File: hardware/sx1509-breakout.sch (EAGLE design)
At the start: 23 parts, among them U1 SX1509

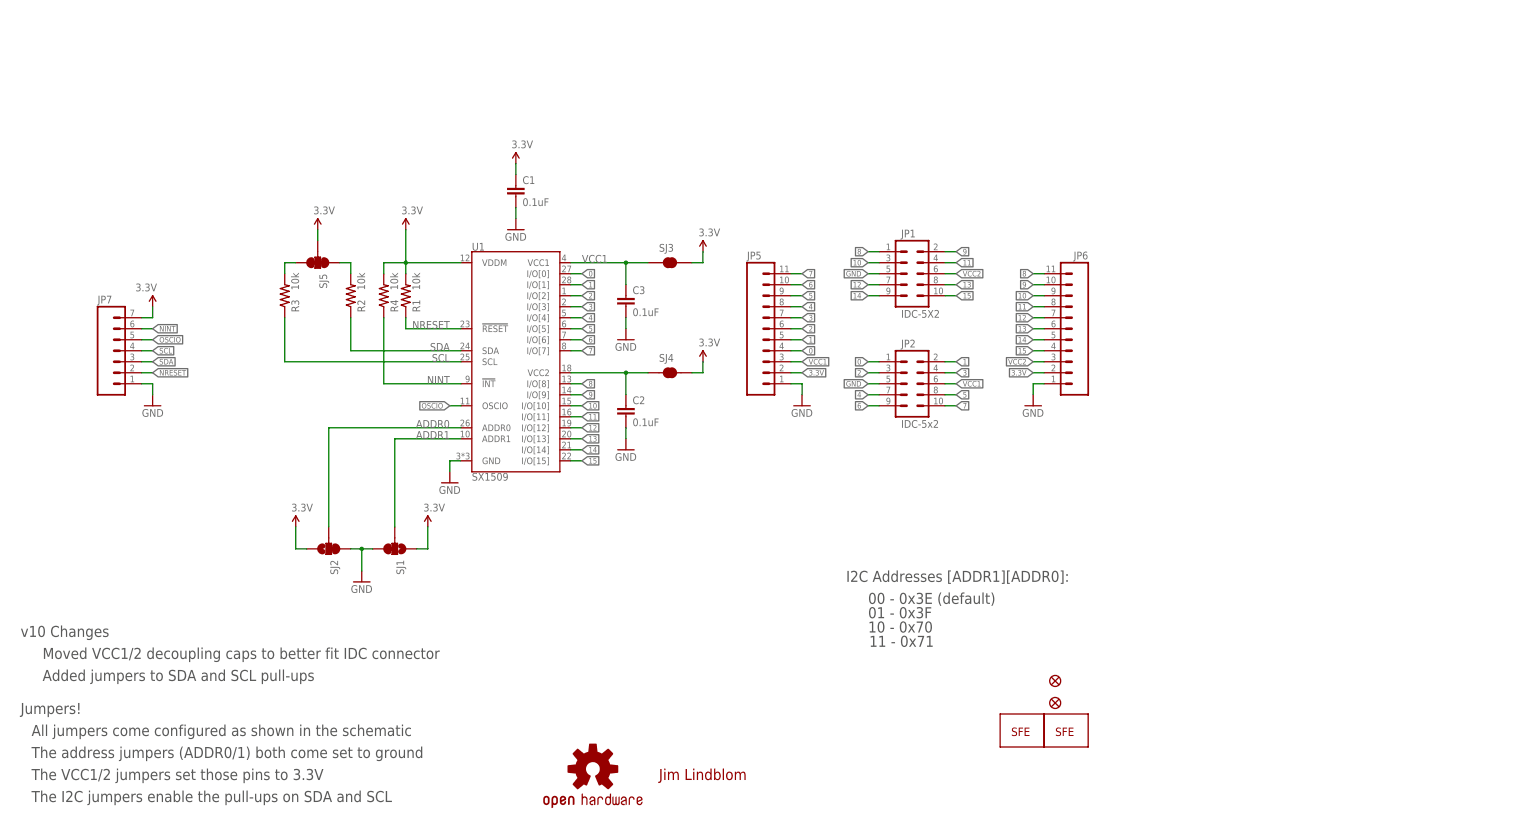
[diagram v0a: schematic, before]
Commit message: Initial commit of v1.1
- Added standoff holes
- Changed I2C headers to match SparkFun standard
- Added I2C pins to both sides to allow cascading boards.
- Updated Eagle libraries
- Updated 0402 packages to 0603.
- Increase fiducial size
- Updated logos
- Added 10k resistors to SJ2 and SJ3.
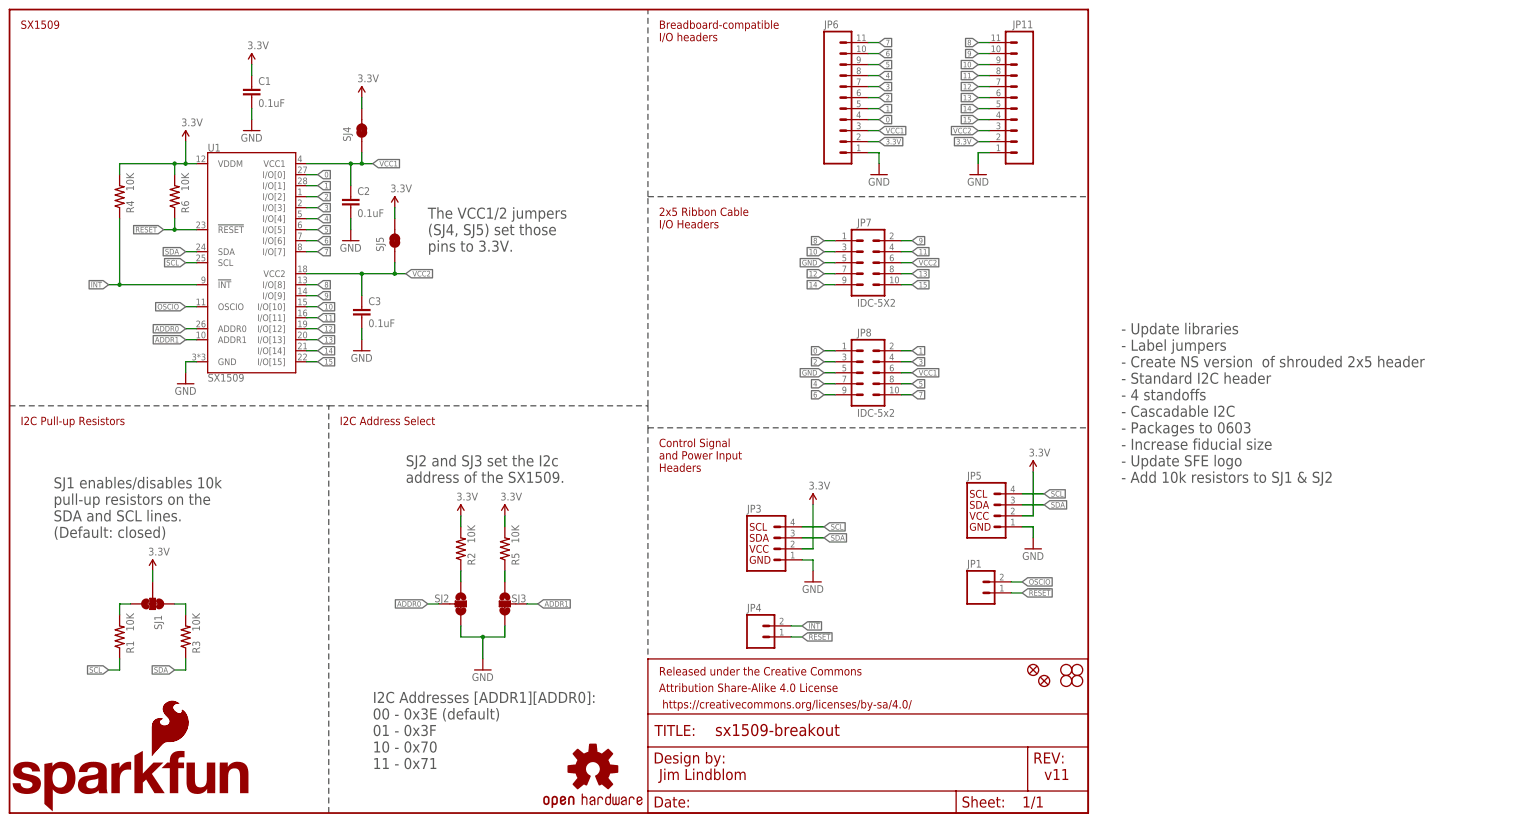
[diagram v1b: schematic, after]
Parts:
- removed JP2: IDC-5x2, SparkFun-Connectors:M05X2SHD_NS
- added FRAME1: (no value), SparkFun-Aesthetics:FRAME-LETTER
- added JP10: FIDUCIAL1X2, SparkFun:FIDUCIAL1X2
- added JP11: (no value), SparkFun-Connectors:M111X11_NO_SILK
- added LOGO1: SFE_LOGO_NAME_FLAME.1_INCH, SparkFun-Aesthetics:SFE_LOGO_NAME_FLAME.1_INCH
- added LOGO2: SFE_LOGO_FLAME.1_INCH, SparkFun-Aesthetics:SFE_LOGO_FLAME.1_INCH
- added R5, R6: 10K, SparkFun-Resistors:10KOHM-1/10W-1%(0603)0603
- added STANDOFF1, STANDOFF2, STANDOFF3, STANDOFF4: STAND-OFF, SparkFun-Electromechanical:STAND-OFF
- C1, C2, C3: device SparkFun-Passives:CAP0402-CAP -> SparkFun-Capacitors:0.1UF-25V(+80/-20%)(0603)
- JP1: value IDC-5X2 -> (none); device SparkFun-Connectors:M05X2SHD_NS -> SparkFun-Connectors:M021X02_NO_SILK
- JP3: value LOGO-SFENEW -> (none); device SparkFun-Aesthetics:LOGO-SFENEW -> SparkFun-Connectors:I2C_STANDARD_NO_SILK
- JP4: value LOGO-SFESK -> (none); device SparkFun-Aesthetics:LOGO-SFESK -> SparkFun-Connectors:M021X02_NO_SILK
- JP5: value M111X11_NO_SILK -> (none); device SparkFun-Connectors:M111X11_NO_SILK -> SparkFun-Connectors:I2C_STANDARD_NO_SILK
- JP6: value M111X11_NO_SILK -> (none)
- JP7: value (none) -> IDC-5X2; device SparkFun-Connectors:M07 -> SparkFun-Connectors:M05X2SHD-NS
- JP8: value FIDUCIALUFIDUCIAL -> IDC-5x2; device SparkFun:FIDUCIALUFIDUCIAL -> SparkFun-Connectors:M05X2SHD-NS
- JP9: value FIDUCIALUFIDUCIAL -> FIDUCIAL1X2; device SparkFun:FIDUCIALUFIDUCIAL -> SparkFun:FIDUCIAL1X2
- R1, R2, R3, R4: value 10k -> 10K; device SparkFun-Passives:RESISTOR0402-RES -> SparkFun-Resistors:10KOHM-1/10W-1%(0603)0603
- SJ1: device SparkFun-Passives:SOLDERJUMPER_2WAYS -> SparkFun-Passives:JUMPER-PAD-3-NC_BY_TRACE
- SJ2: value (none) -> JUMPER-PAD-3-2OF3_NC_BY_TRACE_SMALL; device SparkFun-Passives:SOLDERJUMPER_2WAYS -> SparkFun-Passives:JUMPER-PAD-3-2OF3_NC_BY_TRACE_SMALL
- SJ3: value SOLDERJUMPERNO -> JUMPER-PAD-3-2OF3_NC_BY_TRACE_SMALL; device SparkFun-Passives:SOLDERJUMPERNO -> SparkFun-Passives:JUMPER-PAD-3-2OF3_NC_BY_TRACE_SMALL
- SJ4: value SOLDERJUMPERNO -> JUMPER-PAD-2-NC_BY_TRACE; device SparkFun-Passives:SOLDERJUMPERNO -> SparkFun-Passives:JUMPER-PAD-2-NC_BY_TRACE
- SJ5: value (none) -> JUMPER-PAD-2-NC_BY_TRACE; device SparkFun-Passives:SOLDERJUMPER_2WAYS -> SparkFun-Passives:JUMPER-PAD-2-NC_BY_TRACE
- renumbered U$1 to LOGO3
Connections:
- removed net NINT: JP7.6, R4.1, U1.!INT
- removed net NRESET: JP7.2, R1.1, U1.!RESET
- new net !INT: JP4.2, R4.1, U1.!INT
- new net !RESET: JP1.1, JP4.1, R6.1, U1.!RESET
- new net N$8: R2.1, SJ2.1
- new net N$9: R5.1, SJ3.1
- net 0: now also JP6.4, JP8.1; no longer JP2.1, JP5.4
- net 1: now also JP6.5, JP8.2; no longer JP2.2, JP5.5
- net 10: now also JP11.9, JP7.3; no longer JP1.3, JP6.9
- net 11: now also JP11.8, JP7.4; no longer JP1.4, JP6.8
- net 12: now also JP11.7, JP7.7; no longer JP1.7, JP6.7
- net 13: now also JP11.6, JP7.8; no longer JP1.8, JP6.6
- net 14: now also JP11.5, JP7.9; no longer JP1.9, JP6.5
- net 15: now also JP11.4, JP7.10; no longer JP1.10, JP6.4
- net 2: now also JP6.6, JP8.3; no longer JP2.3, JP5.6
- net 3: now also JP6.7, JP8.4; no longer JP2.4, JP5.7
- net 3.3V: now also JP11.2, JP3.2, R2.2, R5.2, R6.2, SJ1.2; no longer JP7.7, R1.2, SJ1.1, SJ2.3, SJ3.2
- net 4: now also JP6.8, JP8.7; no longer JP2.7, JP5.8
- net 5: now also JP6.9, JP8.8; no longer JP2.8, JP5.9
- net 6: now also JP6.10, JP8.9; no longer JP2.9, JP5.10
- net 7: now also JP6.11, JP8.10; no longer JP2.10, JP5.11
- net 8: now also JP11.11, JP7.1; no longer JP1.1, JP6.11
- net 9: now also JP11.10, JP7.2; no longer JP1.2, JP6.10
- net ADDR1: now also SJ3.2; no longer SJ1.2
- net GND: now also JP11.1, JP3.1, JP7.5, JP8.5, SJ2.3, SJ3.3; no longer JP1.5, JP2.5, JP7.1, SJ1.3, SJ2.1
- net N$1: now also R1.2, SJ1.3; no longer R3.2, SJ5.3
- net N$2: now also R3.2, SJ1.1; no longer R2.2, SJ5.1
- net OSCIO: now also JP1.2; no longer JP7.5
- net SCL: now also JP3.4, JP5.4, R1.1; no longer JP7.4, R3.1
- net SDA: now also JP3.3, JP5.3, R3.1; no longer JP7.3, R2.1
- net VCC1: now also C2.1, JP6.3, JP8.6, SJ4.1; no longer C3.1, JP2.6, JP5.3, SJ3.1
- net VCC2: now also C3.1, JP11.3, JP7.6, SJ5.1; no longer C2.1, JP1.6, JP6.3, SJ4.1
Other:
- note added: "- Update libraries - Label jumpers - Create NS version of shrouded 2x5 header - Standard I2C header - 4 standoffs - Cascadable I2C - Packages to 0603 - Increase fiducial size - Update SFE logo - Add 10k resistors to SJ1 & SJ2"
- note added: "2x5 Ribbon Cable I/O Headers"
- note added: "Breadboard-compatible I/O headers"
- note added: "Control Signal and Power Input Headers"
- note added: "I2C Address Select"
- note added: "I2C Addresses [ADDR1][ADDR0]: 00 - 0x3E (default) 01 - 0x3F 10 - 0x70 11 - 0x71"
- note added: "I2C Pull-up Resistors"
- note added: "SJ1 enables/disables 10k pull-up resistors on the SDA and SCL lines. (Default: closed)"
- note added: "SJ2 and SJ3 set the I2c address of the SX1509."
- note added: "SX1509"
- note added: "The VCC1/2 jumpers (SJ4, SJ5) set those pins to 3.3V."
- note added: "v11"
- note removed: "00 - 0x3E (default)"
- note removed: "01 - 0x3F"
- note removed: "10 - 0x70"
- note removed: "11 - 0x71"
- note removed: "Added jumpers to SDA and SCL pull-ups"
- note removed: "All jumpers come configured as shown in the schematic"
- note removed: "I2C Addresses [ADDR1][ADDR0]:"
- note removed: "Jumpers!"
- note removed: "Moved VCC1/2 decoupling caps to better fit IDC connector"
- note removed: "The I2C jumpers enable the pull-ups on SDA and SCL"
- note removed: "The VCC1/2 jumpers set those pins to 3.3V"
- note removed: "The address jumpers (ADDR0/1) both come set to ground"
- note removed: "v10 Changes"
- moved on the sheet: C1, C2, C3, JP6, R1, R2, R3, R4, U1

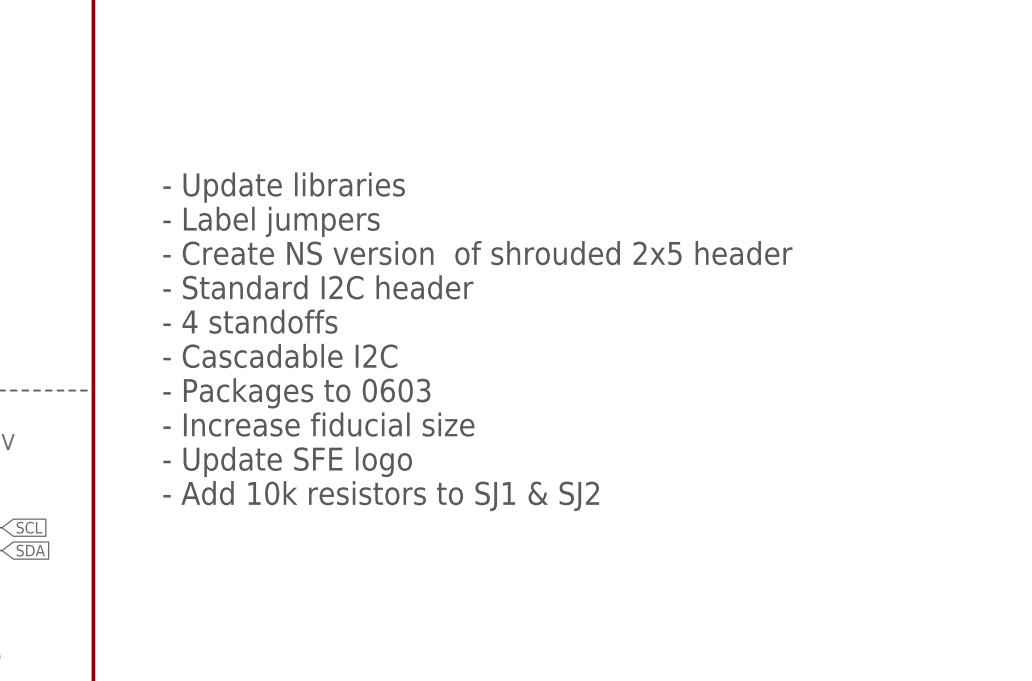
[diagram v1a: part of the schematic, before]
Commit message: Labeling SJ4 and SJ5.
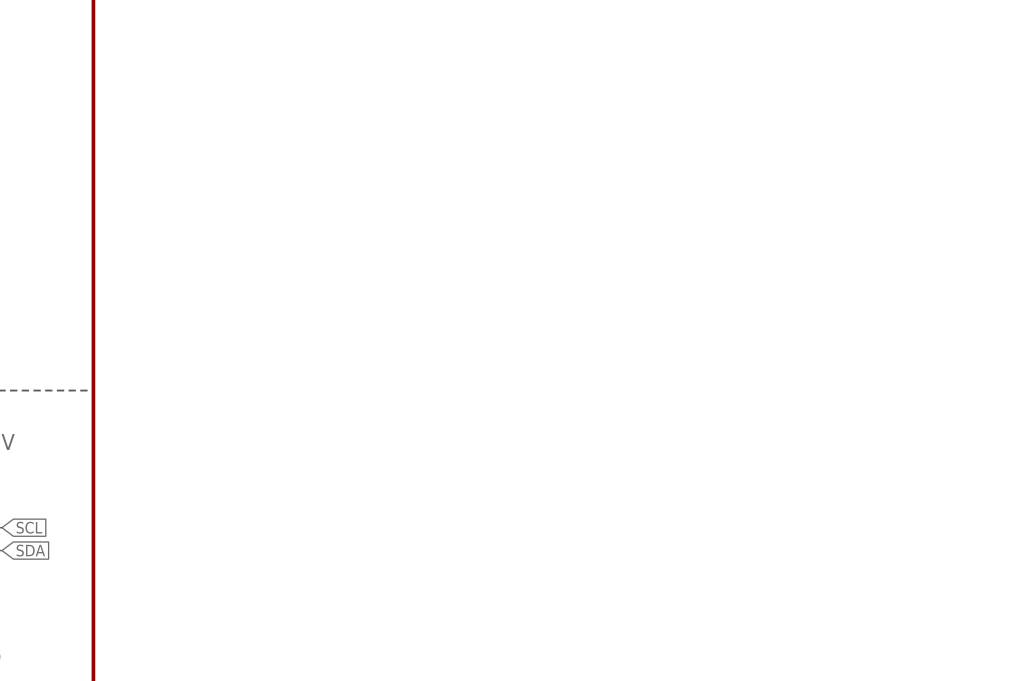
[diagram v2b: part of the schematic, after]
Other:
- note removed: "- Update libraries - Label jumpers - Create NS version of shrouded 2x5 header - Standard I2C header - 4 standoffs - Cascadable I2C - Packages to 0603 - Increase fiducial size - Update SFE logo - Add 10k resistors to SJ1 & SJ2"
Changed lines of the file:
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@@
 <grid distance="0.1" unitdist="inch" unit="inch" style="lines" multiple="1" display="no" altdistance="0.01" altunitdist="inch" altunit="inch"/>
 <layers>
-<layer number="1" name="Top" color="4" fill="1" visible="yes" active="no"/>
-<layer number="2" name="Route2" color="1" fill="3" visible="yes" active="no"/>
-<layer number="3" name="Route3" color="4" fill="3" visible="yes" active="no"/>
-<layer number="4" name="Route4" color="1" fill="4" visible="yes" active="no"/>
-<layer number="5" name="Route5" color="4" fill="4" visible="yes" active="no"/>
-<layer number="6" name="Route6" color="1" fill="8" visible="yes" active="no"/>
-<layer number="7" name="Route7" color="4" fill="8" visible="yes" active="no"/>
-<layer number="8" name="Route8" color="1" fill="2" visible="yes" active="no"/>
-<layer number="9" name="Route9" color="4" fill="2" visible="yes" active="no"/>
-<layer number="10" name="Route10" color="1" fill="7" visible="yes" active="no"/>
-<layer number="11" name="Route11" color="4" fill="7" visible="yes" active="no"/>
-<layer number="12" name="Route12" color="1" fill="5" visible="yes" active="no"/>
-<layer number="13" name="Route13" color="4" fill="5" visible="yes" active="no"/>
-<layer number="14" name="Route14" color="1" fill="6" visible="yes" active="no"/>
-<layer number="15" name="Route15" color="4" fill="6" visible="yes" active="no"/>
-<layer number="16" name="Bottom" color="1" fill="1" visible="yes" active="no"/>
-<layer number="17" name="Pads" color="2" fill="1" visible="yes" active="no"/>
-<layer number="18" name="Vias" color="2" fill="1" visible="yes" active="no"/>
-<layer number="19" name="Unrouted" color="6" fill="1" visible="yes" active="no"/>
-<layer number="20" name="Dimension" color="15" fill="1" visible="yes" active="no"/>
-<layer number="21" name="tPlace" color="16" fill="1" visible="yes" active="no"/>
-<layer number="22" name="bPlace" color="14" fill="1" visible="yes" active="no"/>
-<layer number="23" name="tOrigins" color="15" fill="1" visible="yes" active="no"/>
-<layer number="24" name="bOrigins" color="15" fill="1" visible="yes" active="no"/>
-<layer number="25" name="tNames" color="7" fill="1" visible="yes" active="no"/>
-<layer number="26" name="bNames" color="7" fill="1" visible="yes" active="no"/>
-<layer number="27" name="tValues" color="7" fill="1" visible="yes" active="no"/>
-<layer number="28" name="bValues" color="7" fill="1" visible="yes" active="no"/>
+<layer number="1" name="Top" color="4" fill="1" visible="no" active="no"/>
+<layer number="2" name="Route2" color="1" fill="3" visible="no" active="no"/>
+<layer number="3" name="Route3" color="4" fill="3" visible="no" active="no"/>
+<layer number="4" name="Route4" color="1" fill="4" visible="no" active="no"/>
+<layer number="5" name="Route5" color="4" fill="4" visible="no" active="no"/>
+<layer number="6" name="Route6" color="1" fill="8" visible="no" active="no"/>
+<layer number="7" name="Route7" color="4" fill="8" visible="no" active="no"/>
+<layer number="8" name="Route8" color="1" fill="2" visible="no" active="no"/>
+<layer number="9" name="Route9" color="4" fill="2" visible="no" active="no"/>
+<layer number="10" name="Route10" color="1" fill="7" visible="no" active="no"/>
+<layer number="11" name="Route11" color="4" fill="7" visible="no" active="no"/>
+<layer number="12" name="Route12" color="1" fill="5" visible="no" active="no"/>
+<layer number="13" name="Route13" color="4" fill="5" visible="no" active="no"/>
+<layer number="14" name="Route14" color="1" fill="6" visible="no" active="no"/>
+<layer number="15" name="Route15" color="4" fill="6" visible="no" active="no"/>
+<layer number="16" name="Bottom" color="1" fill="1" visible="no" active="no"/>
+<layer number="17" name="Pads" color="2" fill="1" visible="no" active="no"/>
+<layer number="18" name="Vias" color="2" fill="1" visible="no" active="no"/>
+<layer number="19" name="Unrouted" color="6" fill="1" visible="no" active="no"/>
+<layer number="20" name="Dimension" color="15" fill="1" visible="no" active="no"/>
+<layer number="21" name="tPlace" color="16" fill="1" visible="no" active="no"/>
+<layer number="22" name="bPlace" color="14" fill="1" visible="no" active="no"/>
+<layer number="23" name="tOrigins" color="15" fill="1" visible="no" active="no"/>
+<layer number="24" name="bOrigins" color="15" fill="1" visible="no" active="no"/>
+<layer number="25" name="tNames" color="7" fill="1" visible="no" active="no"/>
+<layer number="26" name="bNames" color="7" fill="1" visible="no" active="no"/>
+<layer number="27" name="tValues" color="7" fill="1" visible="no" active="no"/>
+<layer number="28" name="bValues" color="7" fill="1" visible="no" active="no"/>
 <layer number="29" name="tStop" color="7" fill="3" visible="no" active="no"/>
 <layer number="30" name="bStop" color="7" fill="6" visible="no" active="no"/>
@@
 <layer number="35" name="tGlue" color="7" fill="4" visible="no" active="no"/>
 <layer number="36" name="bGlue" color="7" fill="5" visible="no" active="no"/>
-<layer number="37" name="tTest" color="7" fill="1" visible="yes" active="no"/>
-<layer number="38" name="bTest" color="7" fill="1" visible="yes" active="no"/>
+<layer number="37" name="tTest" color="7" fill="1" visible="no" active="no"/>
+<layer number="38" name="bTest" color="7" fill="1" visible="no" active="no"/>
 <layer number="39" name="tKeepout" color="4" fill="11" visible="no" active="no"/>
 <layer number="40" name="bKeepout" color="1" fill="11" visible="no" active="no"/>
@@
 <layer number="44" name="Drills" color="7" fill="1" visible="no" active="no"/>
 <layer number="45" name="Holes" color="7" fill="1" visible="no" active="no"/>
-<layer number="46" name="Milling" color="3" fill="1" visible="yes" active="no"/>
-<layer number="47" name="Measures" color="7" fill="1" visible="yes" active="no"/>
-<layer number="48" name="Document" color="7" fill="1" visible="yes" active="no"/>
-<layer number="49" name="Reference" color="13" fill="1" visible="yes" active="no"/>
-<layer number="50" name="dxf" color="7" fill="1" visible="yes" active="no"/>
-<layer number="51" name="tDocu" color="6" fill="1" visible="yes" active="no"/>
-<layer number="52" name="bDocu" color="7" fill="1" visible="yes" active="no"/>
-<layer number="53" name="tGND_GNDA" color="7" fill="9" visible="yes" active="no"/>
-<layer number="54" name="bGND_GNDA" color="1" fill="9" visible="yes" active="no"/>
-<layer number="56" name="wert" color="7" fill="1" visible="yes" active="no"/>
-<layer number="57" name="tCAD" color="7" fill="1" visible="yes" active="no"/>
-<layer number="59" name="tCarbon" color="7" fill="1" visible="yes" active="no"/>
-<layer number="60" name="bCarbon" color="7" fill="1" visible="yes" active="no"/>
+<layer number="46" name="Milling" color="3" fill="1" visible="no" active="no"/>
+<layer number="47" name="Measures" color="7" fill="1" visible="no" active="no"/>
+<layer number="48" name="Document" color="7" fill="1" visible="no" active="no"/>
+<layer number="49" name="Reference" color="13" fill="1" visible="no" active="no"/>
+<layer number="50" name="dxf" color="7" fill="1" visible="no" active="no"/>
+<layer number="51" name="tDocu" color="6" fill="1" visible="no" active="no"/>
+<layer number="52" name="bDocu" color="7" fill="1" visible="no" active="no"/>
+<layer number="53" name="tGND_GNDA" color="7" fill="9" visible="no" active="no"/>
+<layer number="54" name="bGND_GNDA" color="1" fill="9" visible="no" active="no"/>
+<layer number="56" name="wert" color="7" fill="1" visible="no" active="no"/>
+<layer number="57" name="tCAD" color="7" fill="1" visible="no" active="no"/>
+<layer number="59" name="tCarbon" color="7" fill="1" visible="no" active="no"/>
+<layer number="60" name="bCarbon" color="7" fill="1" visible="no" active="no"/>
 <layer number="90" name="Modules" color="5" fill="1" visible="yes" active="yes"/>
 <layer number="91" name="Nets" color="2" fill="1" visible="yes" active="yes"/>
@@
 11 - 0x71</text>
 <text x="238.76" y="7.62" size="2.54" layer="94">v11</text>
-<text x="256.54" y="76.2" size="2.54" layer="97">- Update libraries
-- Label jumpers
-- Create NS version  of shrouded 2x5 header
-- Standard I2C header
-- 4 standoffs
-- Cascadable I2C
-- Packages to 0603
-- Increase fiducial size
-- Update SFE logo
-- Add 10k resistors to SJ1 &amp; SJ2</text>
 <text x="10.16" y="63.5" size="2.54" layer="97">SJ1 enables/disables 10k
 pull-up resistors on the
